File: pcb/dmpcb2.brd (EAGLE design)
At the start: 100 x 100 mm, 71 parts, among them IC1 7805DT, IC2 L293D, IC4 LM358D, IC5 LM358D, J7 SJ-3523-SMT-TR, Q1 IRF530, Q2 IRF530

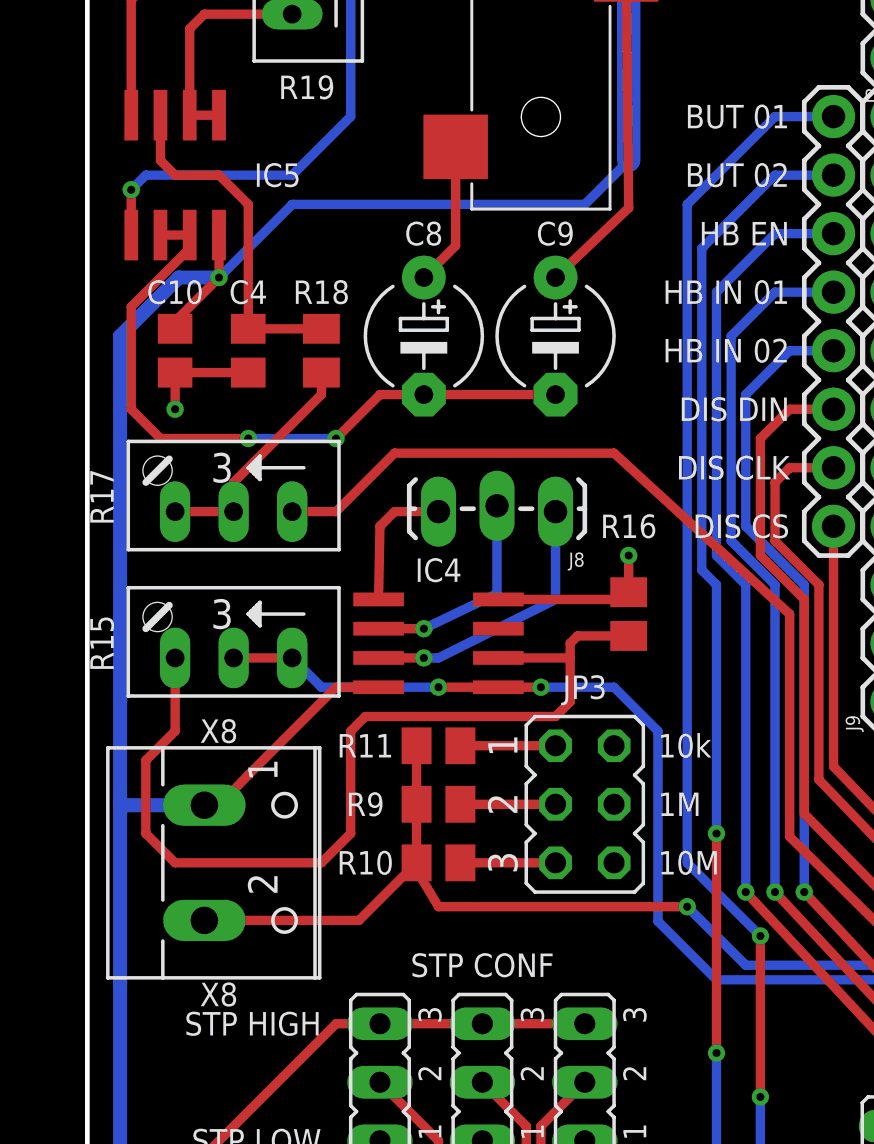
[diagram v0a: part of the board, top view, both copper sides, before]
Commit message: moved bypass caps
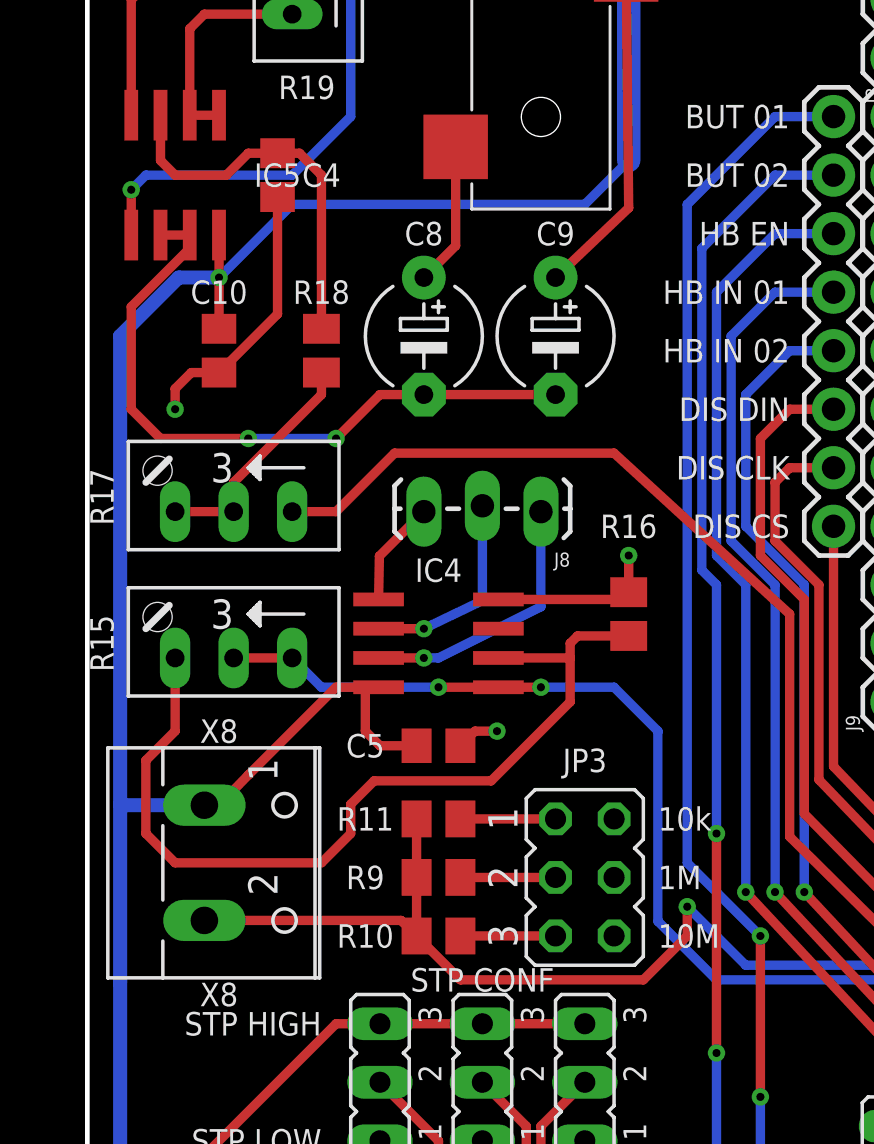
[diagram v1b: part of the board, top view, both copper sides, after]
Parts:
- added C5: 100nf, rcl:C0805
- moved C4 7.73 mm to (8.26, 84.5)
- moved JP3 3.17 mm to (21.6, 54.0)
- moved R10 3.17 mm to (15.2, 51.4)
- moved R11 3.17 mm to (15.2, 56.5)
- moved R9 3.17 mm to (15.2, 54.0)
- moved C10 1.90 mm to (5.71, 76.8)
- moved J8 0.64 mm to (19.7, 69.8)
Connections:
- net +5V: now also C5.1
- net GND: now also C5.2
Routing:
- net GND: track 57.7 -> 66.5 mm, vias 7 -> 8
- net +5V: track 361.6 -> 365.2 mm
- net N$63: track 40.9 -> 39.1 mm
- net N$68: track 15.1 -> 16.7 mm
- net N$20: track 5.98 -> 4.61 mm
- net SENSORPORT: track 108.1 -> 109.0 mm

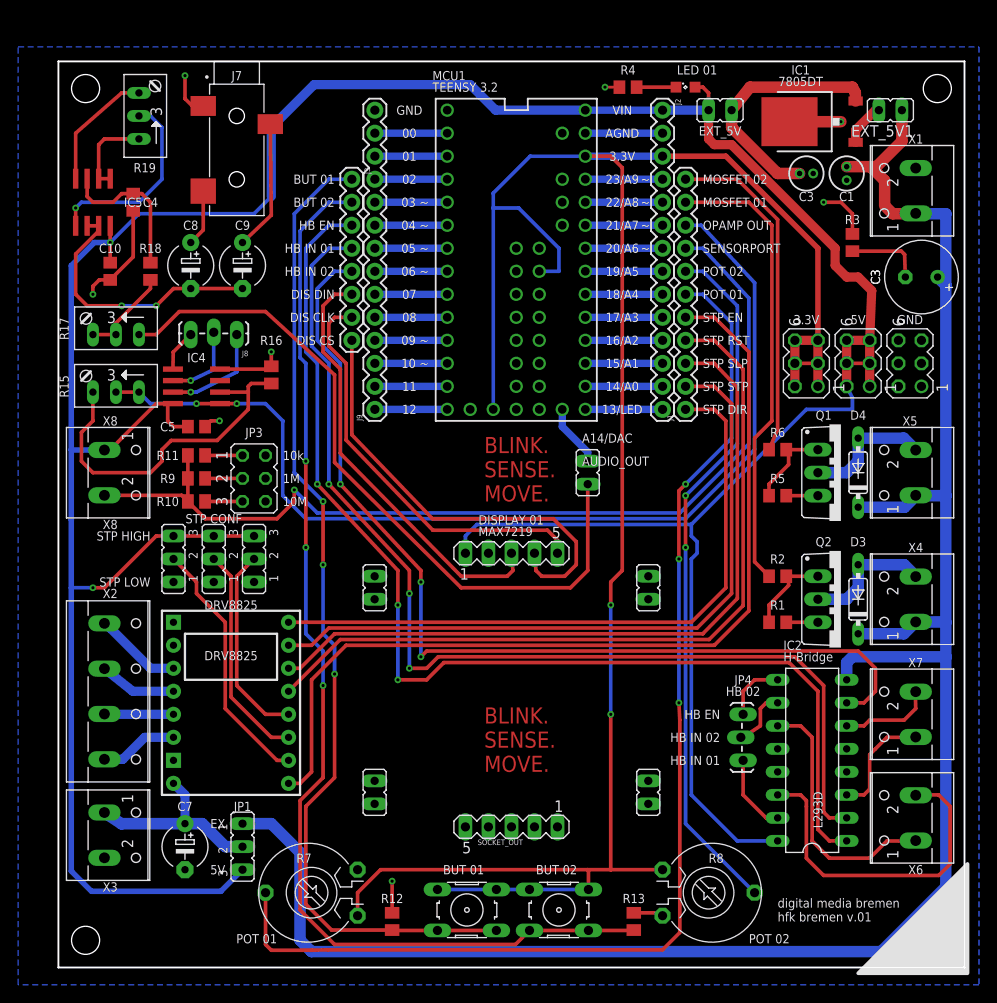
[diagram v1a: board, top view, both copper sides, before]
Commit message: added support for second display, but only is possible at the time
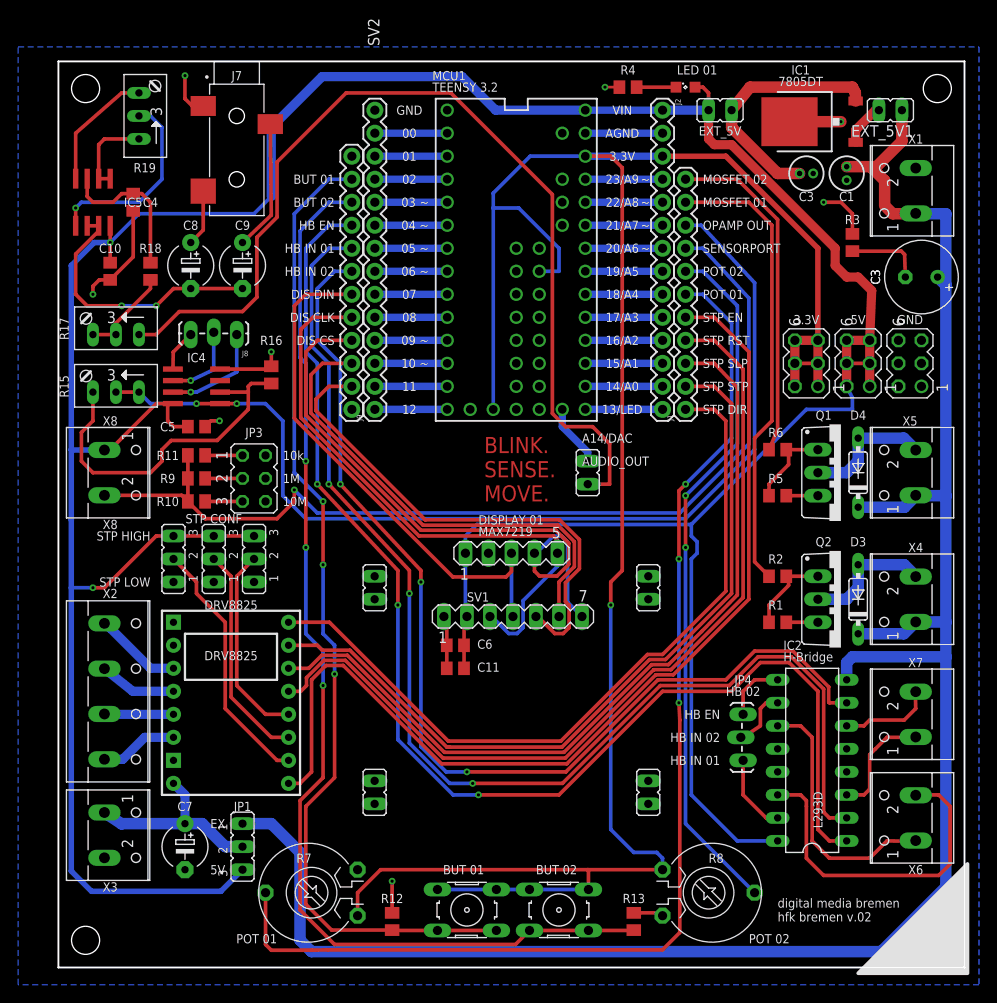
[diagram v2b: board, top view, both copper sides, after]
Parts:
- removed J3: (no value), SparkFun-Connectors:1X08
- removed SOCKET_OUT: (no value), con-lstb:MA05-1
- added C11: 10uf, rcl:C0805
- added C6: 100nf, rcl:C0805
- added SV1: (no value), con-lstb:MA07-1
- added SV2: (no value), SparkFun-Connectors:1X12
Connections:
- new net OLEDDC: SV1.6, SV2.10
- new net OLEDRES: SV1.5, SV2.11
- net +5V: now also C11.1, C6.1, SV1.2
- net BUTTON01: now also SV2.2; no longer J3.1
- net BUTTON02: now also SV2.3; no longer J3.2
- net GND: now also C11.2, C6.2, SV1.1
- net H-BRDIGE_A_02: now also SV2.6; no longer J3.5
- net H-BRIDGE_A_01: now also SV2.5; no longer J3.4
- net H-BRIDGE_A_EN: now also SV2.4; no longer J3.3
- net MAX7219CLK: now also SV1.3, SV2.8; no longer J3.7
- net MAX7219CS: now also SV1.7, SV2.9; no longer J3.8
- net MAX7219DIN: now also SV1.4, SV2.7; no longer J3.6
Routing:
- net OLEDRES: track 0.00 -> 56.0 mm
- net OLEDDC: track 0.00 -> 53.2 mm
- net BETTERAUDIOOUT: track 79.0 -> 107.5 mm
- net MAX7219CS: track 49.9 -> 69.9 mm
- net MAX7219CLK: track 46.0 -> 65.8 mm
- net H-BRIDGE_A_01: track 118.3 -> 133.4 mm
- net H-BRIDGE_A_EN: track 125.2 -> 139.6 mm
- net +5V: track 365.2 -> 378.9 mm
- net MAX7219DIN: track 47.7 -> 59.8 mm
- net DRV8825DIR: track 73.2 -> 84.3 mm
- net H-BRDIGE_A_02: track 107.3 -> 116.7 mm
- net DRV8825STEP: track 78.1 -> 87.4 mm
- net DRV8825RST: track 87.8 -> 96.8 mm
- net DRV8825SLP: track 82.9 -> 91.5 mm
- net DRV8825EN: track 101.8 -> 110.0 mm
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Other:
- board text added: "digital media bremen hfk bremen v.02"
- board text removed: "digital media bremen hfk bremen v.01"

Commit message: added second jack for midi, not too sure if position is good. thinking about putting pads on the bottom of the board and making the jack optional?
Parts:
- added J3: SJ-3523-SMT-TR, SJ-3523-SMT-TR:CUI_SJ-3523-SMT-TR
- moved JP1 3.81 mm to (20.3, 17.1), turned to 180 degrees
- moved J7 2.54 mm to (17.1, 94.0)
- moved C9 0.64 mm to (19.7, 77.5)
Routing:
- net BETTERAUDIOOUT: track 107.5 -> 112.6 mm
- net GND: track 72.4 -> 76.1 mm, vias 8 -> 12
- net +5V: track 378.9 -> 381.9 mm
- net N$73: track 14.4 -> 13.6 mm
- net VMOT: track 21.6 -> 22.4 mm
- net N$72: track 29.6 -> 29.0 mm
- net V+: track 224.1 -> 223.6 mm

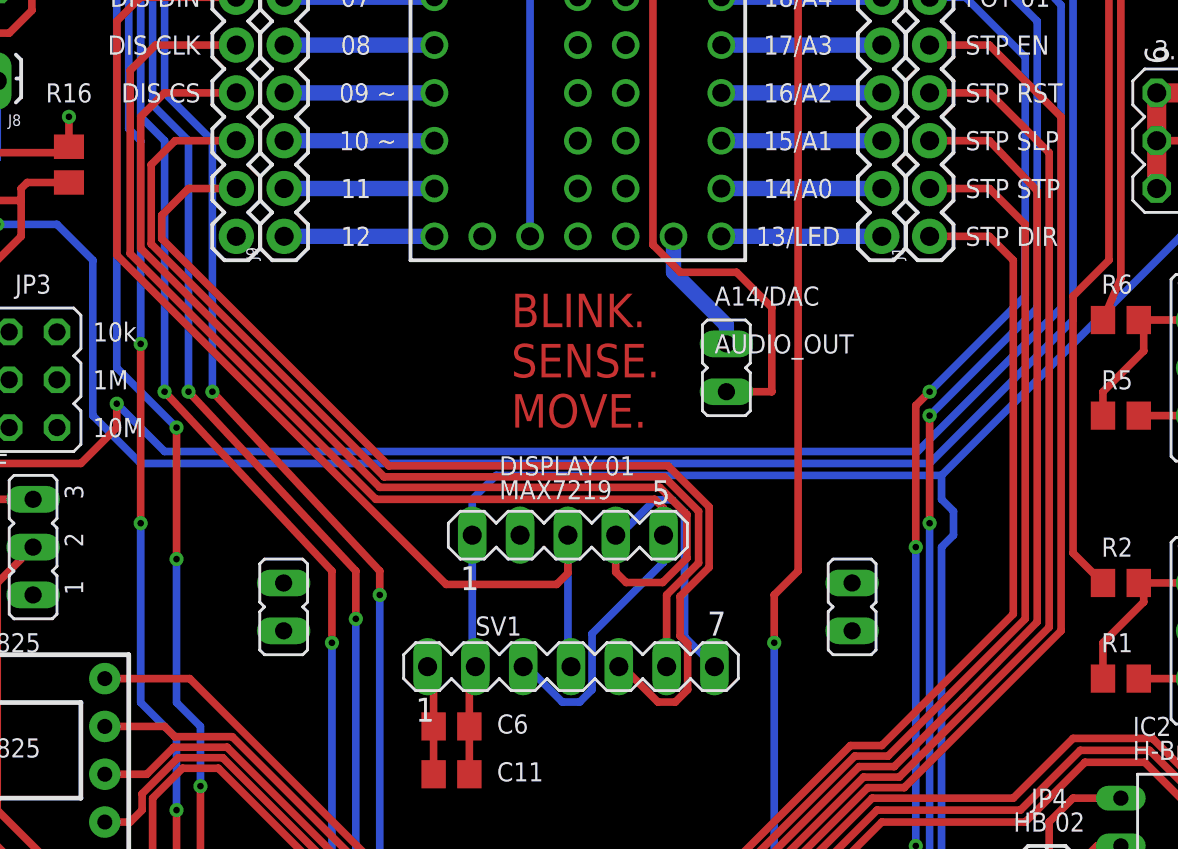
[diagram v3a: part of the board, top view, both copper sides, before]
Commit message: moved second display a bit upwards
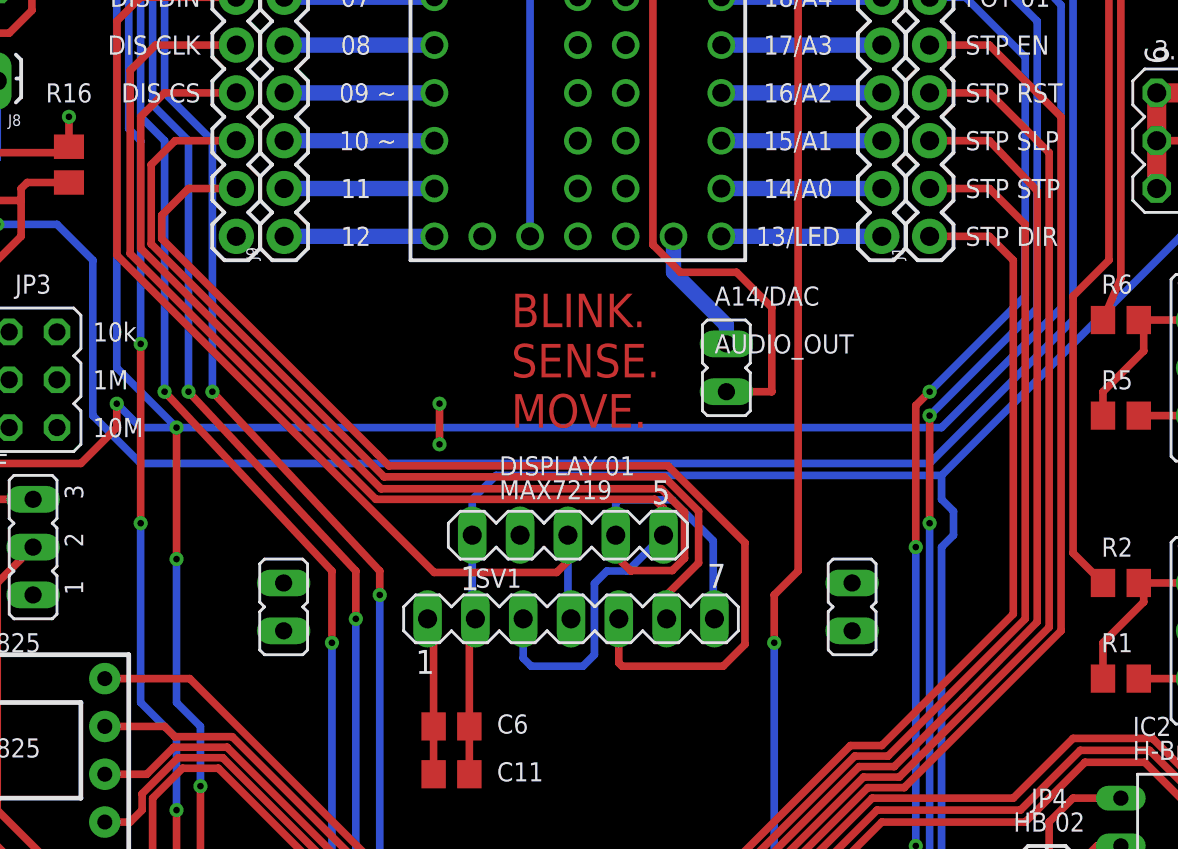
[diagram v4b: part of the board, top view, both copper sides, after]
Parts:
- moved SV1 2.54 mm to (50.2, 41.3)
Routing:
- net MAX7219DIN: track 59.8 -> 56.4 mm
- net MAX7219CS: track 69.9 -> 67.1 mm
- net GND: track 76.1 -> 78.7 mm
- net OLEDDC: track 53.2 -> 50.6 mm
- net OLEDRES: track 56.0 -> 58.5 mm
- net N$21: track 0.00 -> 2.16 mm, vias 0 -> 2
- net SENSORPORT: track 109.0 -> 108.0 mm

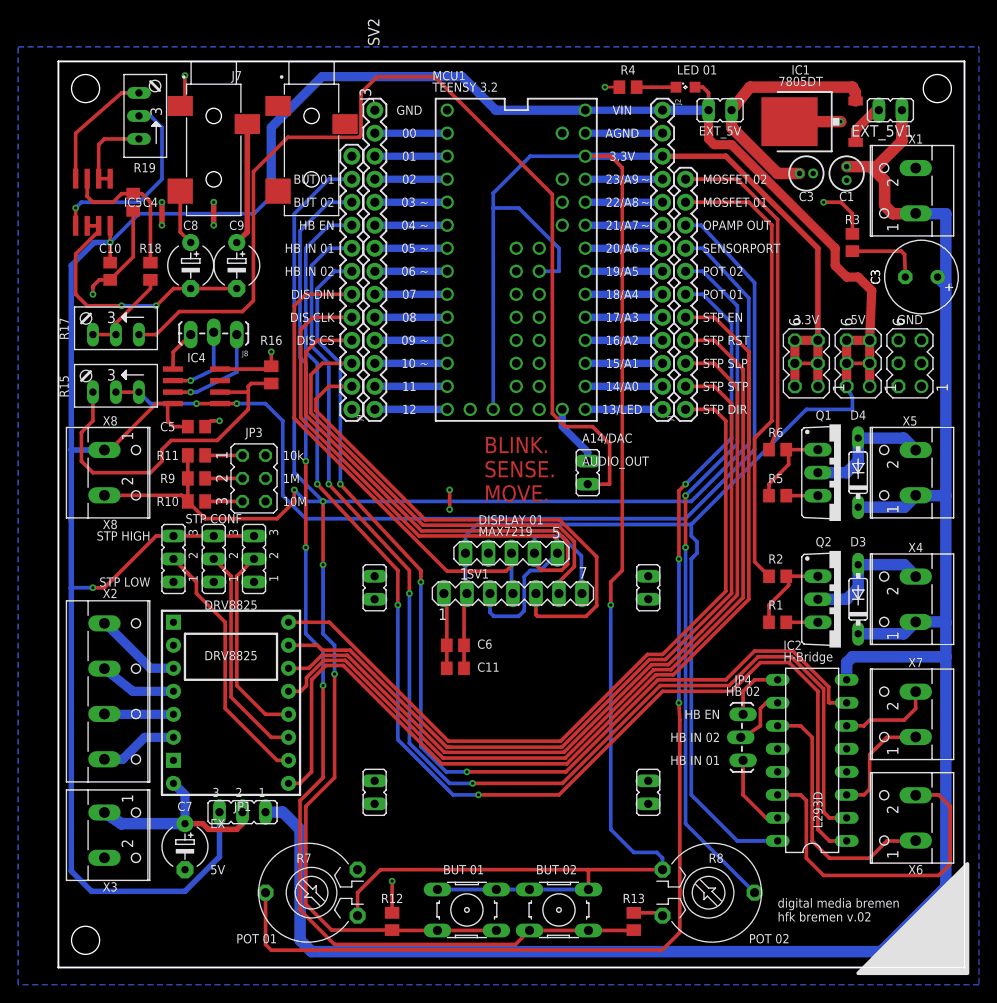
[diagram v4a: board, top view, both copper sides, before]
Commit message: removed second 3.5mm jack, drc comes back clean
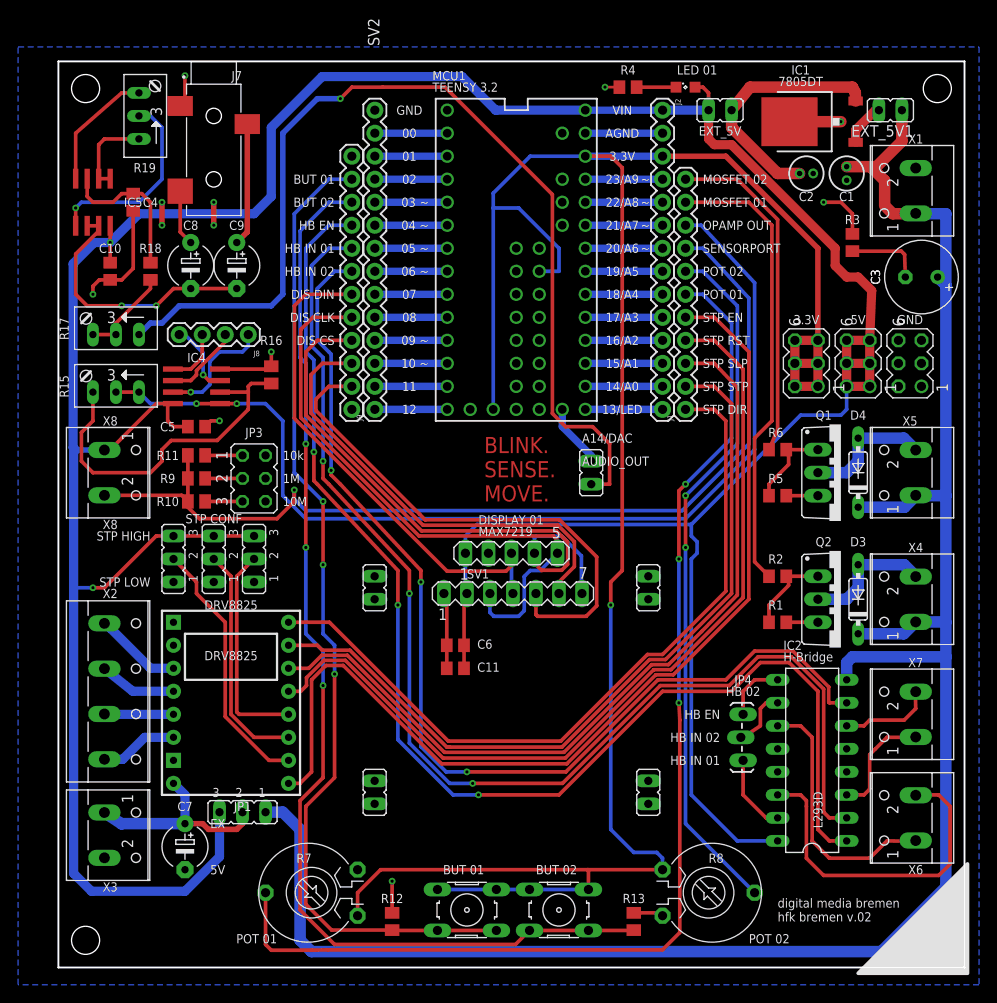
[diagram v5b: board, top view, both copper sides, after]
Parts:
- removed J3: SJ-3523-SMT-TR, SJ-3523-SMT-TR:CUI_SJ-3523-SMT-TR
- J8: device SparkFun-Connectors:1X03_LOCK_LONGPADS -> SparkFun-Connectors:1X04
- moved J8 1.27 mm to (21.0, 69.8)
- moved 14/DAC 0.38 mm to (58.8, 54.6)
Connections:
- net OPAMPIN: now also J8.4
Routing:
- net OPAMPIN: track 0.00 -> 8.02 mm, vias 0 -> 1
- net 3.3V: track 247.4 -> 249.9 mm
- net N$21: track 2.16 -> 0.00 mm, vias 2 -> 0
- net BETTERAUDIOOUT: track 112.6 -> 110.6 mm, vias 0 -> 1
- net SENSORPORT: track 108.0 -> 109.8 mm
- net N$57: track 21.8 -> 23.5 mm
- net N$20: track 4.61 -> 6.30 mm
- net N$75: track 11.7 -> 13.2 mm
- net N$58: track 24.2 -> 25.3 mm
- net +5V: track 381.9 -> 382.7 mm
- net GND: track 78.7 -> 79.4 mm
- net N$59: track 28.2 -> 28.8 mm
- net N$70: track 8.90 -> 8.62 mm, vias 1 -> 0
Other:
- board text added: "C2"
